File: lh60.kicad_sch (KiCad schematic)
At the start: 0 parts

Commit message: feat(sch): add production keyboard matrix
Co-authored-by: TRAE CLI <noreply@bytedance.com>
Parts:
- added D1, D10, D11, D12, D13, D14, D15, D16, D17, D18, D19, D2, D20, D21, D22, D23, D24, D25, D26, D27, D28, D29, D3, D30, D31, D32, D33, D34, D35, D36, D37, D38, D39, D4, D40, D41, D42, D43, D44, D45, D46, D47, D48, D49, D5, D50, D51, D52, D53, D54, D55, D56, D57, D58, D59, D6, D60, D61, D62, D63, D64, D65, D66, D67, D68, D69, D7, D70, D8, D9: 1N4148WS, lh60-core:D_SOD-323_Bottom, symbol lh60-core:MatrixDiode
- added SW1: r0_esc_1u, lh60-sockets:Gateron-LP-or-ChocV1-Hotswap-Socket-1U, symbol lh60-core:KeySwitch
- added SW10: r0_9_1u, lh60-sockets:Gateron-LP-or-ChocV1-Hotswap-Socket-1U, symbol lh60-core:KeySwitch
- added SW11: r0_0_1u, lh60-sockets:Gateron-LP-or-ChocV1-Hotswap-Socket-1U, symbol lh60-core:KeySwitch
- added SW12: r0_minus_1u, lh60-sockets:Gateron-LP-or-ChocV1-Hotswap-Socket-1U, symbol lh60-core:KeySwitch
- added SW13: r0_equal_1u, lh60-sockets:Gateron-LP-or-ChocV1-Hotswap-Socket-1U, symbol lh60-core:KeySwitch
- added SW14: r0_top_2u, lh60-sockets:Gateron-LP-Hotswap-Socket-2U, symbol lh60-core:KeySwitch
- added SW15: r0_top_split_left_fn_1u, lh60-sockets:Gateron-LP-Hotswap-Socket-1U, symbol lh60-core:KeySwitch
- added SW16: r0_top_split_right_1u, lh60-sockets:Gateron-LP-Hotswap-Socket-1U, symbol lh60-core:KeySwitch
- added SW17: r1_tab_1.5u, lh60-sockets:Gateron-LP-or-ChocV1-Hotswap-Socket-1.5U, symbol lh60-core:KeySwitch
- added SW18: r1_q_1u, lh60-sockets:Gateron-LP-or-ChocV1-Hotswap-Socket-1U, symbol lh60-core:KeySwitch
- added SW19: r1_w_1u, lh60-sockets:Gateron-LP-or-ChocV1-Hotswap-Socket-1U, symbol lh60-core:KeySwitch
- added SW2: r0_1_1u, lh60-sockets:Gateron-LP-or-ChocV1-Hotswap-Socket-1U, symbol lh60-core:KeySwitch
- added SW20: r1_e_1u, lh60-sockets:Gateron-LP-or-ChocV1-Hotswap-Socket-1U, symbol lh60-core:KeySwitch
- added SW21: r1_r_1u, lh60-sockets:Gateron-LP-or-ChocV1-Hotswap-Socket-1U, symbol lh60-core:KeySwitch
- added SW22: r1_t_1u, lh60-sockets:Gateron-LP-or-ChocV1-Hotswap-Socket-1U, symbol lh60-core:KeySwitch
- added SW23: r1_y_1u, lh60-sockets:Gateron-LP-or-ChocV1-Hotswap-Socket-1U, symbol lh60-core:KeySwitch
- added SW24: r1_u_1u, lh60-sockets:Gateron-LP-or-ChocV1-Hotswap-Socket-1U, symbol lh60-core:KeySwitch
- added SW25: r1_i_1u, lh60-sockets:Gateron-LP-or-ChocV1-Hotswap-Socket-1U, symbol lh60-core:KeySwitch
- added SW26: r1_o_1u, lh60-sockets:Gateron-LP-or-ChocV1-Hotswap-Socket-1U, symbol lh60-core:KeySwitch
- added SW27: r1_p_1u, lh60-sockets:Gateron-LP-or-ChocV1-Hotswap-Socket-1U, symbol lh60-core:KeySwitch
- added SW28: r1_left_bracket_1u, lh60-sockets:Gateron-LP-or-ChocV1-Hotswap-Socket-1U, symbol lh60-core:KeySwitch
- added SW29: r1_right_bracket_1u, lh60-sockets:Gateron-LP-or-ChocV1-Hotswap-Socket-1U, symbol lh60-core:KeySwitch
- added SW3: r0_2_1u, lh60-sockets:Gateron-LP-or-ChocV1-Hotswap-Socket-1U, symbol lh60-core:KeySwitch
- added SW30: r1_backslash_1.5u, lh60-sockets:Gateron-LP-or-ChocV1-Hotswap-Socket-1.5U, symbol lh60-core:KeySwitch
- added SW31: r2_caps_1.75u, lh60-sockets:Gateron-LP-or-ChocV1-Hotswap-Socket-1.75U, symbol lh60-core:KeySwitch
- added SW32: r2_a_1u, lh60-sockets:Gateron-LP-or-ChocV1-Hotswap-Socket-1U, symbol lh60-core:KeySwitch
- added SW33: r2_s_1u, lh60-sockets:Gateron-LP-or-ChocV1-Hotswap-Socket-1U, symbol lh60-core:KeySwitch
- added SW34: r2_d_1u, lh60-sockets:Gateron-LP-or-ChocV1-Hotswap-Socket-1U, symbol lh60-core:KeySwitch
- added SW35: r2_f_1u, lh60-sockets:Gateron-LP-or-ChocV1-Hotswap-Socket-1U, symbol lh60-core:KeySwitch
- added SW36: r2_g_1u, lh60-sockets:Gateron-LP-or-ChocV1-Hotswap-Socket-1U, symbol lh60-core:KeySwitch
- added SW37: r2_h_1u, lh60-sockets:Gateron-LP-or-ChocV1-Hotswap-Socket-1U, symbol lh60-core:KeySwitch
- added SW38: r2_j_1u, lh60-sockets:Gateron-LP-or-ChocV1-Hotswap-Socket-1U, symbol lh60-core:KeySwitch
- added SW39: r2_k_1u, lh60-sockets:Gateron-LP-or-ChocV1-Hotswap-Socket-1U, symbol lh60-core:KeySwitch
- added SW4: r0_3_1u, lh60-sockets:Gateron-LP-or-ChocV1-Hotswap-Socket-1U, symbol lh60-core:KeySwitch
- added SW40: r2_l_1u, lh60-sockets:Gateron-LP-or-ChocV1-Hotswap-Socket-1U, symbol lh60-core:KeySwitch
- added SW41: r2_semicolon_1u, lh60-sockets:Gateron-LP-or-ChocV1-Hotswap-Socket-1U, symbol lh60-core:KeySwitch
- added SW42: r2_quote_1u, lh60-sockets:Gateron-LP-or-ChocV1-Hotswap-Socket-1U, symbol lh60-core:KeySwitch
- added SW43: r2_enter_ansi_2.25u, lh60-sockets:Gateron-LP-Hotswap-Socket-2.25U, symbol lh60-core:KeySwitch
- added SW44: r2_enter_split_left_fn_1u, lh60-sockets:Gateron-LP-Hotswap-Socket-1U, symbol lh60-core:KeySwitch
- added SW45: r2_enter_split_right_1.25u, lh60-sockets:Gateron-LP-Hotswap-Socket-1.25U, symbol lh60-core:KeySwitch
- added SW46: r3_lshift_split_left_fn_1u, lh60-sockets:Gateron-LP-Hotswap-Socket-1U, symbol lh60-core:KeySwitch
- added SW47: r3_lshift_2.25u, lh60-sockets:Gateron-LP-Hotswap-Socket-2.25U, symbol lh60-core:KeySwitch
- added SW48: r3_lshift_split_1.25u, lh60-sockets:Gateron-LP-Hotswap-Socket-1.25U, symbol lh60-core:KeySwitch
- added SW49: r3_z_1u, lh60-sockets:Gateron-LP-or-ChocV1-Hotswap-Socket-1U, symbol lh60-core:KeySwitch
- added SW5: r0_4_1u, lh60-sockets:Gateron-LP-or-ChocV1-Hotswap-Socket-1U, symbol lh60-core:KeySwitch
- added SW50: r3_x_1u, lh60-sockets:Gateron-LP-or-ChocV1-Hotswap-Socket-1U, symbol lh60-core:KeySwitch
- added SW51: r3_c_1u, lh60-sockets:Gateron-LP-or-ChocV1-Hotswap-Socket-1U, symbol lh60-core:KeySwitch
- added SW52: r3_v_1u, lh60-sockets:Gateron-LP-or-ChocV1-Hotswap-Socket-1U, symbol lh60-core:KeySwitch
- added SW53: r3_b_1u, lh60-sockets:Gateron-LP-or-ChocV1-Hotswap-Socket-1U, symbol lh60-core:KeySwitch
- added SW54: r3_n_1u, lh60-sockets:Gateron-LP-or-ChocV1-Hotswap-Socket-1U, symbol lh60-core:KeySwitch
- added SW55: r3_m_1u, lh60-sockets:Gateron-LP-or-ChocV1-Hotswap-Socket-1U, symbol lh60-core:KeySwitch
- added SW56: r3_comma_1u, lh60-sockets:Gateron-LP-or-ChocV1-Hotswap-Socket-1U, symbol lh60-core:KeySwitch
- added SW57: r3_period_1u, lh60-sockets:Gateron-LP-or-ChocV1-Hotswap-Socket-1U, symbol lh60-core:KeySwitch
- added SW58: r3_slash_1u, lh60-sockets:Gateron-LP-or-ChocV1-Hotswap-Socket-1U, symbol lh60-core:KeySwitch
- added SW59: r3_rshift_2.75u, lh60-sockets:Gateron-LP-Hotswap-Socket-2.75U, symbol lh60-core:KeySwitch
- added SW6: r0_5_1u, lh60-sockets:Gateron-LP-or-ChocV1-Hotswap-Socket-1U, symbol lh60-core:KeySwitch
- added SW60: r3_rshift_left_1.75u, lh60-sockets:Gateron-LP-Hotswap-Socket-1.75U, symbol lh60-core:KeySwitch
- added SW61: r3_rshift_right_fn_1u, lh60-sockets:Gateron-LP-Hotswap-Socket-1U, symbol lh60-core:KeySwitch
- added SW62: r3_rshift_left_fn_1u, lh60-sockets:Gateron-LP-Hotswap-Socket-1U, symbol lh60-core:KeySwitch
- added SW63: r3_rshift_right_1.75u, lh60-sockets:Gateron-LP-Hotswap-Socket-1.75U, symbol lh60-core:KeySwitch
- added SW64: r4_left_ctrl_1.25u, lh60-sockets:Gateron-LP-or-ChocV1-Hotswap-Socket-1.25U, symbol lh60-core:KeySwitch
- added SW65: r4_left_win_1.25u, lh60-sockets:Gateron-LP-or-ChocV1-Hotswap-Socket-1.25U, symbol lh60-core:KeySwitch
- added SW66: r4_left_alt_1.25u, lh60-sockets:Gateron-LP-or-ChocV1-Hotswap-Socket-1.25U, symbol lh60-core:KeySwitch
- added SW67: r4_space_2.25u, lh60-sockets:Gateron-LP-or-ChocV1-Hotswap-Socket-2.25U, symbol lh60-core:KeySwitch
- added SW68: r4_fn_1u, lh60-sockets:Gateron-LP-or-ChocV1-Hotswap-Socket-1U, symbol lh60-core:KeySwitch
- added SW69: r4_left_1u, lh60-sockets:Gateron-LP-or-ChocV1-Hotswap-Socket-1U, symbol lh60-core:KeySwitch
- added SW7: r0_6_1u, lh60-sockets:Gateron-LP-or-ChocV1-Hotswap-Socket-1U, symbol lh60-core:KeySwitch
- added SW70: r4_down_1u, lh60-sockets:Gateron-LP-or-ChocV1-Hotswap-Socket-1U, symbol lh60-core:KeySwitch
- added SW71: r4_up_1u, lh60-sockets:Gateron-LP-or-ChocV1-Hotswap-Socket-1U, symbol lh60-core:KeySwitch
- added SW72: r4_right_1u, lh60-sockets:Gateron-LP-or-ChocV1-Hotswap-Socket-1U, symbol lh60-core:KeySwitch
- added SW73: r4_right_fn_1u, lh60-sockets:Gateron-LP-or-ChocV1-Hotswap-Socket-1U, symbol lh60-core:KeySwitch
- added SW74: r4_right_alt_1u, lh60-sockets:Gateron-LP-or-ChocV1-Hotswap-Socket-1U, symbol lh60-core:KeySwitch
- added SW75: r4_right_win_1u, lh60-sockets:Gateron-LP-or-ChocV1-Hotswap-Socket-1U, symbol lh60-core:KeySwitch
- added SW76: r4_right_ctrl_1u, lh60-sockets:Gateron-LP-or-ChocV1-Hotswap-Socket-1U, symbol lh60-core:KeySwitch
- added SW8: r0_7_1u, lh60-sockets:Gateron-LP-or-ChocV1-Hotswap-Socket-1U, symbol lh60-core:KeySwitch
- added SW9: r0_8_1u, lh60-sockets:Gateron-LP-or-ChocV1-Hotswap-Socket-1U, symbol lh60-core:KeySwitch
- added TP1: VSYS, lh60-core:TestPoint_Pad_D1.5mm_Bottom, symbol lh60-core:TestPoint
- added TP10: COL6, lh60-core:TestPoint_Pad_D1.5mm_Bottom, symbol lh60-core:TestPoint
- added TP11: COL7, lh60-core:TestPoint_Pad_D1.5mm_Bottom, symbol lh60-core:TestPoint
- added TP12: COL8, lh60-core:TestPoint_Pad_D1.5mm_Bottom, symbol lh60-core:TestPoint
- added TP13: COL9, lh60-core:TestPoint_Pad_D1.5mm_Bottom, symbol lh60-core:TestPoint
- added TP14: ROW0, lh60-core:TestPoint_Pad_D1.5mm_Bottom, symbol lh60-core:TestPoint
- added TP15: ROW1, lh60-core:TestPoint_Pad_D1.5mm_Bottom, symbol lh60-core:TestPoint
- added TP16: ROW2, lh60-core:TestPoint_Pad_D1.5mm_Bottom, symbol lh60-core:TestPoint
- added TP17: ROW3, lh60-core:TestPoint_Pad_D1.5mm_Bottom, symbol lh60-core:TestPoint
- added TP18: ROW4, lh60-core:TestPoint_Pad_D1.5mm_Bottom, symbol lh60-core:TestPoint
- added TP19: ROW5, lh60-core:TestPoint_Pad_D1.5mm_Bottom, symbol lh60-core:TestPoint
- added TP2: 3V3, lh60-core:TestPoint_Pad_D1.5mm_Bottom, symbol lh60-core:TestPoint
- added TP20: ROW6, lh60-core:TestPoint_Pad_D1.5mm_Bottom, symbol lh60-core:TestPoint
- added TP21: GP27, lh60-core:TestPoint_Pad_D1.5mm_Bottom, symbol lh60-core:TestPoint
- added TP22: GP28, lh60-core:TestPoint_Pad_D1.5mm_Bottom, symbol lh60-core:TestPoint
- added TP23: GP29, lh60-core:TestPoint_Pad_D1.5mm_Bottom, symbol lh60-core:TestPoint
- added TP3: GND, lh60-core:TestPoint_Pad_D1.5mm_Bottom, symbol lh60-core:TestPoint
- added TP4: COL0, lh60-core:TestPoint_Pad_D1.5mm_Bottom, symbol lh60-core:TestPoint
- added TP5: COL1, lh60-core:TestPoint_Pad_D1.5mm_Bottom, symbol lh60-core:TestPoint
- added TP6: COL2, lh60-core:TestPoint_Pad_D1.5mm_Bottom, symbol lh60-core:TestPoint
- added TP7: COL3, lh60-core:TestPoint_Pad_D1.5mm_Bottom, symbol lh60-core:TestPoint
- added TP8: COL4, lh60-core:TestPoint_Pad_D1.5mm_Bottom, symbol lh60-core:TestPoint
- added TP9: COL5, lh60-core:TestPoint_Pad_D1.5mm_Bottom, symbol lh60-core:TestPoint
- added U1: RP2040-Tiny, lh60-mcu:MCU_RP2040-Tiny_SMD, symbol lh60-mcu:RP2040-Tiny
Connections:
- new net 3V3: TP2.1 (TP), U1.21 (3V3)
- new net COL0: D1.2 (A), D11.2 (A), D21.2 (A), D31.2 (A), D41.2 (A), D51.2 (A), D61.2 (A), TP4.1 (TP), U1.1 (GP0)
- new net COL1: D12.2 (A), D2.2 (A), D22.2 (A), D32.2 (A), D42.2 (A), D52.2 (A), D62.2 (A), TP5.1 (TP), U1.2 (GP1)
- new net COL2: D13.2 (A), D23.2 (A), D3.2 (A), D33.2 (A), D43.2 (A), D53.2 (A), D63.2 (A), TP6.1 (TP), U1.3 (GP2)
- new net COL3: D14.2 (A), D24.2 (A), D34.2 (A), D4.2 (A), D44.2 (A), D54.2 (A), D64.2 (A), TP7.1 (TP), U1.4 (GP3)
- new net COL4: D15.2 (A), D25.2 (A), D35.2 (A), D45.2 (A), D5.2 (A), D55.2 (A), D65.2 (A), TP8.1 (TP), U1.5 (GP4)
- new net COL5: D16.2 (A), D26.2 (A), D36.2 (A), D46.2 (A), D56.2 (A), D6.2 (A), D66.2 (A), TP9.1 (TP), U1.6 (GP5)
- new net COL6: D17.2 (A), D27.2 (A), D37.2 (A), D47.2 (A), D57.2 (A), D67.2 (A), D7.2 (A), TP10.1 (TP), U1.7 (GP6)
- new net COL7: D18.2 (A), D28.2 (A), D38.2 (A), D48.2 (A), D58.2 (A), D68.2 (A), D8.2 (A), TP11.1 (TP), U1.8 (GP7)
- new net COL8: D19.2 (A), D29.2 (A), D39.2 (A), D49.2 (A), D59.2 (A), D69.2 (A), D9.2 (A), TP12.1 (TP), U1.9 (GP8)
- new net COL9: D10.2 (A), D20.2 (A), D30.2 (A), D40.2 (A), D50.2 (A), D60.2 (A), D70.2 (A), TP13.1 (TP), U1.10 (GP9)
- new net GND: TP3.1 (TP), U1.22 (GND)
- new net GP27: TP21.1 (TP), U1.18 (GP27)
- new net GP28: TP22.1 (TP), U1.19 (GP28)
- new net GP29: TP23.1 (TP), U1.20 (GP29)
- new net KEY_00: D1.1 (K), SW1.1
- new net KEY_01: D2.1 (K), SW2.1
- new net KEY_02: D3.1 (K), SW3.1
- new net KEY_03: D4.1 (K), SW4.1
- new net KEY_04: D5.1 (K), SW5.1
- new net KEY_05: D6.1 (K), SW6.1
- new net KEY_06: D7.1 (K), SW7.1
- new net KEY_07: D8.1 (K), SW8.1
- new net KEY_08: D9.1 (K), SW9.1
- new net KEY_09: D10.1 (K), SW10.1
- new net KEY_10: D11.1 (K), SW11.1
- new net KEY_11: D12.1 (K), SW12.1
- new net KEY_12: D13.1 (K), SW13.1
- new net KEY_13: D14.1 (K), SW14.1, SW16.1
- new net KEY_14: D15.1 (K), SW15.1
- new net KEY_15: D16.1 (K), SW17.1
- new net KEY_16: D17.1 (K), SW18.1
- new net KEY_17: D18.1 (K), SW19.1
- new net KEY_18: D19.1 (K), SW20.1
- new net KEY_19: D20.1 (K), SW21.1
- new net KEY_20: D21.1 (K), SW22.1
- new net KEY_21: D22.1 (K), SW23.1
- new net KEY_22: D23.1 (K), SW24.1
- new net KEY_23: D24.1 (K), SW25.1
- new net KEY_24: D25.1 (K), SW26.1
- new net KEY_25: D26.1 (K), SW27.1
- new net KEY_26: D27.1 (K), SW28.1
- new net KEY_27: D28.1 (K), SW29.1
- new net KEY_28: D29.1 (K), SW30.1
- new net KEY_29: D30.1 (K), SW31.1
- new net KEY_30: D31.1 (K), SW32.1
- new net KEY_31: D32.1 (K), SW33.1
- new net KEY_32: D33.1 (K), SW34.1
- new net KEY_33: D34.1 (K), SW35.1
- new net KEY_34: D35.1 (K), SW36.1
- new net KEY_35: D36.1 (K), SW37.1
- new net KEY_36: D37.1 (K), SW38.1
- new net KEY_37: D38.1 (K), SW39.1
- new net KEY_38: D39.1 (K), SW40.1
- new net KEY_39: D40.1 (K), SW41.1
- new net KEY_40: D41.1 (K), SW42.1
- new net KEY_41: D42.1 (K), SW43.1, SW45.1
- new net KEY_42: D43.1 (K), SW44.1
- new net KEY_43: D44.1 (K), SW46.1
- new net KEY_44: D45.1 (K), SW47.1, SW48.1
- new net KEY_45: D46.1 (K), SW49.1
- new net KEY_46: D47.1 (K), SW50.1
- new net KEY_47: D48.1 (K), SW51.1
- new net KEY_48: D49.1 (K), SW52.1
- new net KEY_49: D50.1 (K), SW53.1
- new net KEY_50: D51.1 (K), SW54.1
- new net KEY_51: D52.1 (K), SW55.1
- new net KEY_52: D53.1 (K), SW56.1
- new net KEY_53: D54.1 (K), SW57.1
- new net KEY_54: D55.1 (K), SW58.1
- new net KEY_55: D56.1 (K), SW59.1, SW60.1, SW63.1
- new net KEY_56: D57.1 (K), SW61.1, SW62.1
- new net KEY_57: D58.1 (K), SW64.1
- new net KEY_58: D59.1 (K), SW65.1
- new net KEY_59: D60.1 (K), SW66.1
- new net KEY_60: D61.1 (K), SW67.1
- new net KEY_61: D62.1 (K), SW68.1
- new net KEY_62: D63.1 (K), SW69.1
- new net KEY_63: D64.1 (K), SW70.1
- new net KEY_64: D65.1 (K), SW71.1
- new net KEY_65: D66.1 (K), SW72.1
- new net KEY_66: D67.1 (K), SW73.1
- new net KEY_67: D68.1 (K), SW74.1
- new net KEY_68: D69.1 (K), SW75.1
- new net KEY_69: D70.1 (K), SW76.1
- new net ROW0: SW1.2, SW10.2, SW2.2, SW3.2, SW4.2, SW5.2, SW6.2, SW7.2, SW8.2, SW9.2, TP14.1 (TP), U1.11 (GP10)
- new net ROW1: SW11.2, SW12.2, SW13.2, SW14.2, SW15.2, SW16.2, SW17.2, SW18.2, SW19.2, SW20.2, SW21.2, TP15.1 (TP), U1.12 (GP11)
- new net ROW2: SW22.2, SW23.2, SW24.2, SW25.2, SW26.2, SW27.2, SW28.2, SW29.2, SW30.2, SW31.2, TP16.1 (TP), U1.13 (GP12)
- new net ROW3: SW32.2, SW33.2, SW34.2, SW35.2, SW36.2, SW37.2, SW38.2, SW39.2, SW40.2, SW41.2, TP17.1 (TP), U1.14 (GP13)
- new net ROW4: SW42.2, SW43.2, SW44.2, SW45.2, SW46.2, SW47.2, SW48.2, SW49.2, SW50.2, SW51.2, SW52.2, SW53.2, TP18.1 (TP), U1.15 (GP14)
- new net ROW5: SW54.2, SW55.2, SW56.2, SW57.2, SW58.2, SW59.2, SW60.2, SW61.2, SW62.2, SW63.2, SW64.2, SW65.2, SW66.2, TP19.1 (TP), U1.16 (GP15)
- new net ROW6: SW67.2, SW68.2, SW69.2, SW70.2, SW71.2, SW72.2, SW73.2, SW74.2, SW75.2, SW76.2, TP20.1 (TP), U1.17 (GP26)
- new net VSYS: TP1.1 (TP), U1.23 (VSYS)

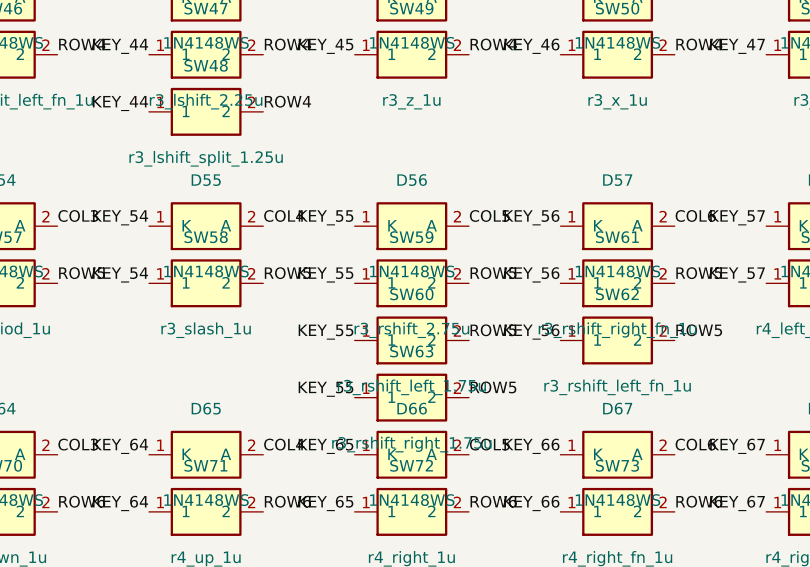
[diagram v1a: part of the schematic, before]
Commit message: refactor(layout): retire RShift 2.75u option
Remove the retired SW59 schematic path while preserving later switch references, refresh production region reports, and update layout documentation and verification gates for the 75-socket contract.

Co-authored-by: TRAE CLI <noreply@bytedance.com>
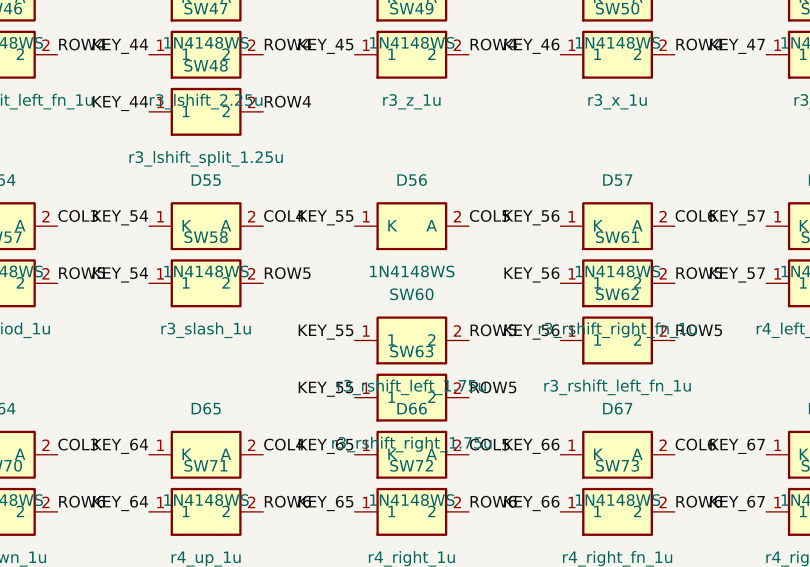
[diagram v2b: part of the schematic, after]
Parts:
- removed SW59: r3_rshift_2.75u, lh60-sockets:Gateron-LP-Hotswap-Socket-2.75U, symbol lh60-core:KeySwitch
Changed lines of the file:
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@@
 )
   (label "ROW5"
-    (at 135.89 148.59 0)
-    (effects
-      (font
-        (size 1.27 1.27))
-      (justify left bottom))
-)
-  (label "ROW5"
     (at 135.89 154.94 0)
     (effects
@@
 )
   (label "KEY_55"
-    (at 123.19 148.59 180)
-    (effects
-      (font
-        (size 1.27 1.27))
-      (justify right bottom))
-)
-  (label "KEY_55"
     (at 123.19 154.94 180)
     (effects
@@
           (unit 1)))))
   (symbol
-    (lib_id "lh60-core:KeySwitch")
-    (at 129.54 148.59 0)
-    (unit 1)
-    (in_bom yes)
-    (on_board yes)
-    (dnp no)
-    (property "Reference" "SW59"
-      (at 129.54 143.51 0)
-      (effects
-        (font
-          (size 1.27 1.27))))
-    (property "Value" "r3_rshift_2.75u"
-      (at 129.54 153.67 0)
-      (effects
-        (font
-          (size 1.27 1.27))))
-    (property "Footprint" "lh60-sockets:Gateron-LP-Hotswap-Socket-2.75U"
-      (at 129.54 148.59 0)
-      (hide yes)
-      (effects
-        (font
-          (size 1.27 1.27))))
-    (property "Datasheet" ""
-      (at 129.54 148.59 0)
-      (hide yes)
-      (effects
-        (font
-          (size 1.27 1.27))))
-    (instances
-      (project "lh60"
-        (path "/1ff94ced-4ad0-4573-85e6-3ea048ef8c2d"
-          (reference "SW59")
-          (unit 1)))))
-  (symbol

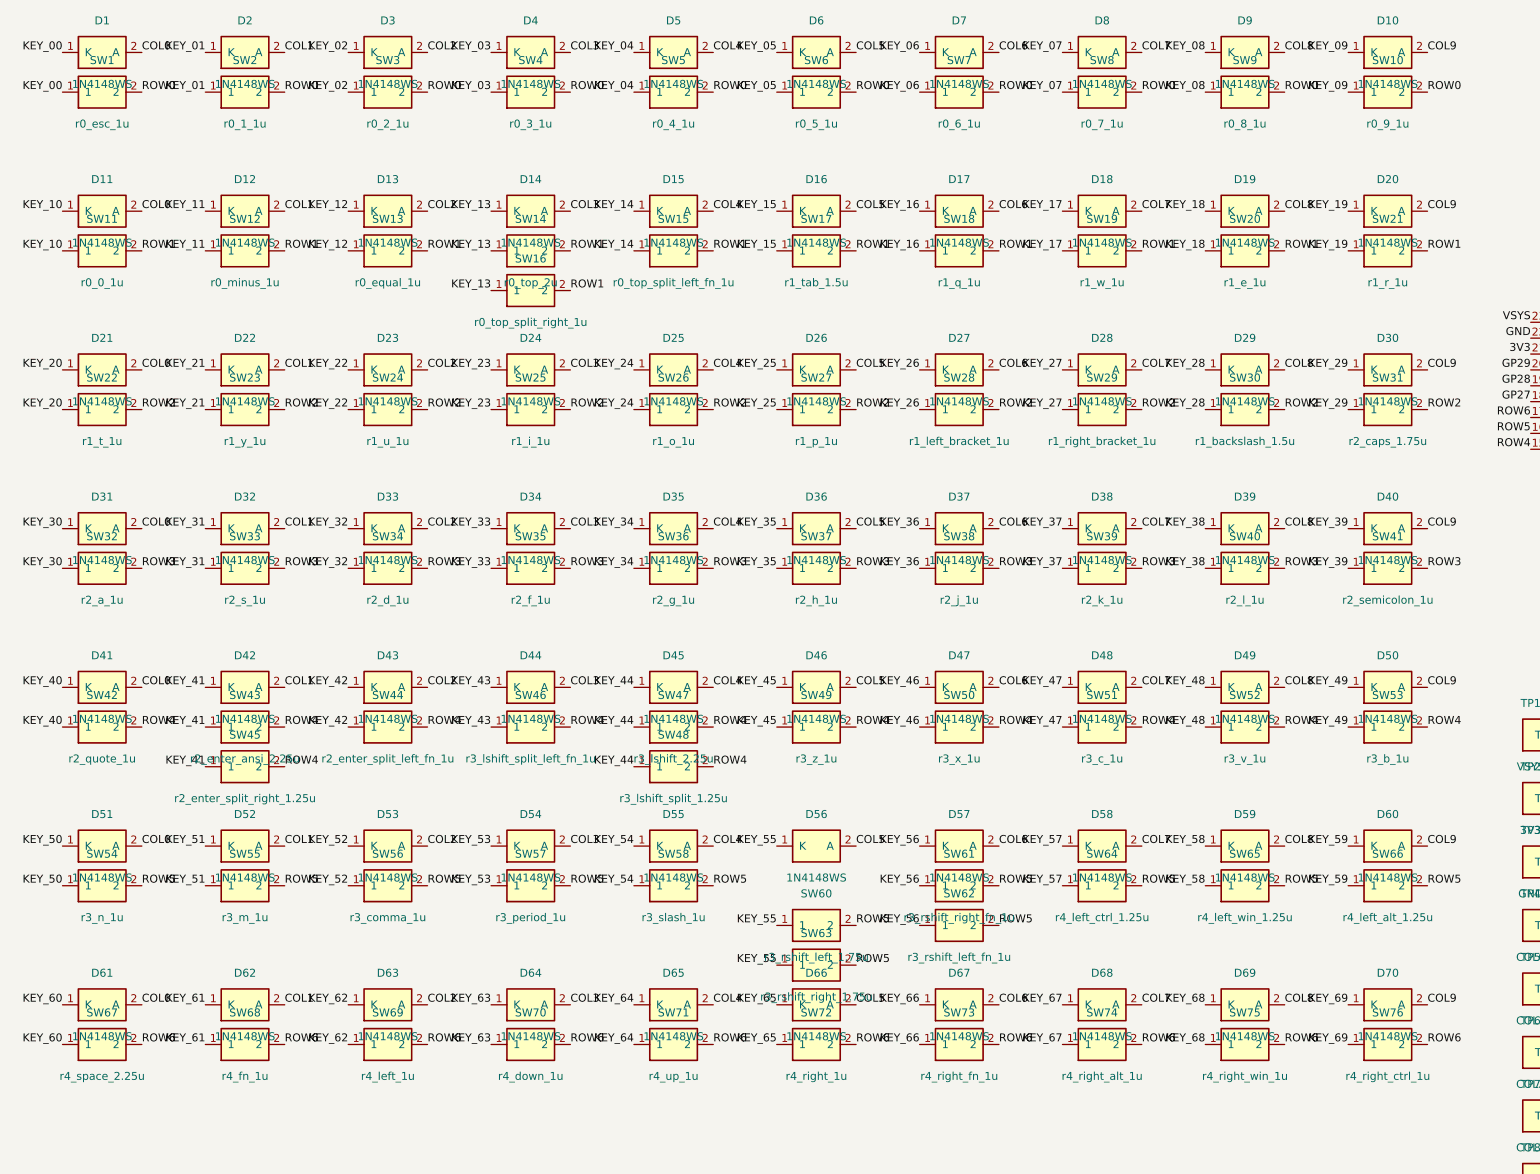
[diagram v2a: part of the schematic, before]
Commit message: refactor(schematic): use default switch and diode symbols
Replace all placed switches with Switch:SW_Push and all matrix diodes with Device:D while preserving references, values, footprints, placement, and connectivity. Remove the retired project-local symbol definitions and keep support symbols and custom footprints in lh60-core.

Co-authored-by: TRAE CLI <noreply@bytedance.com>
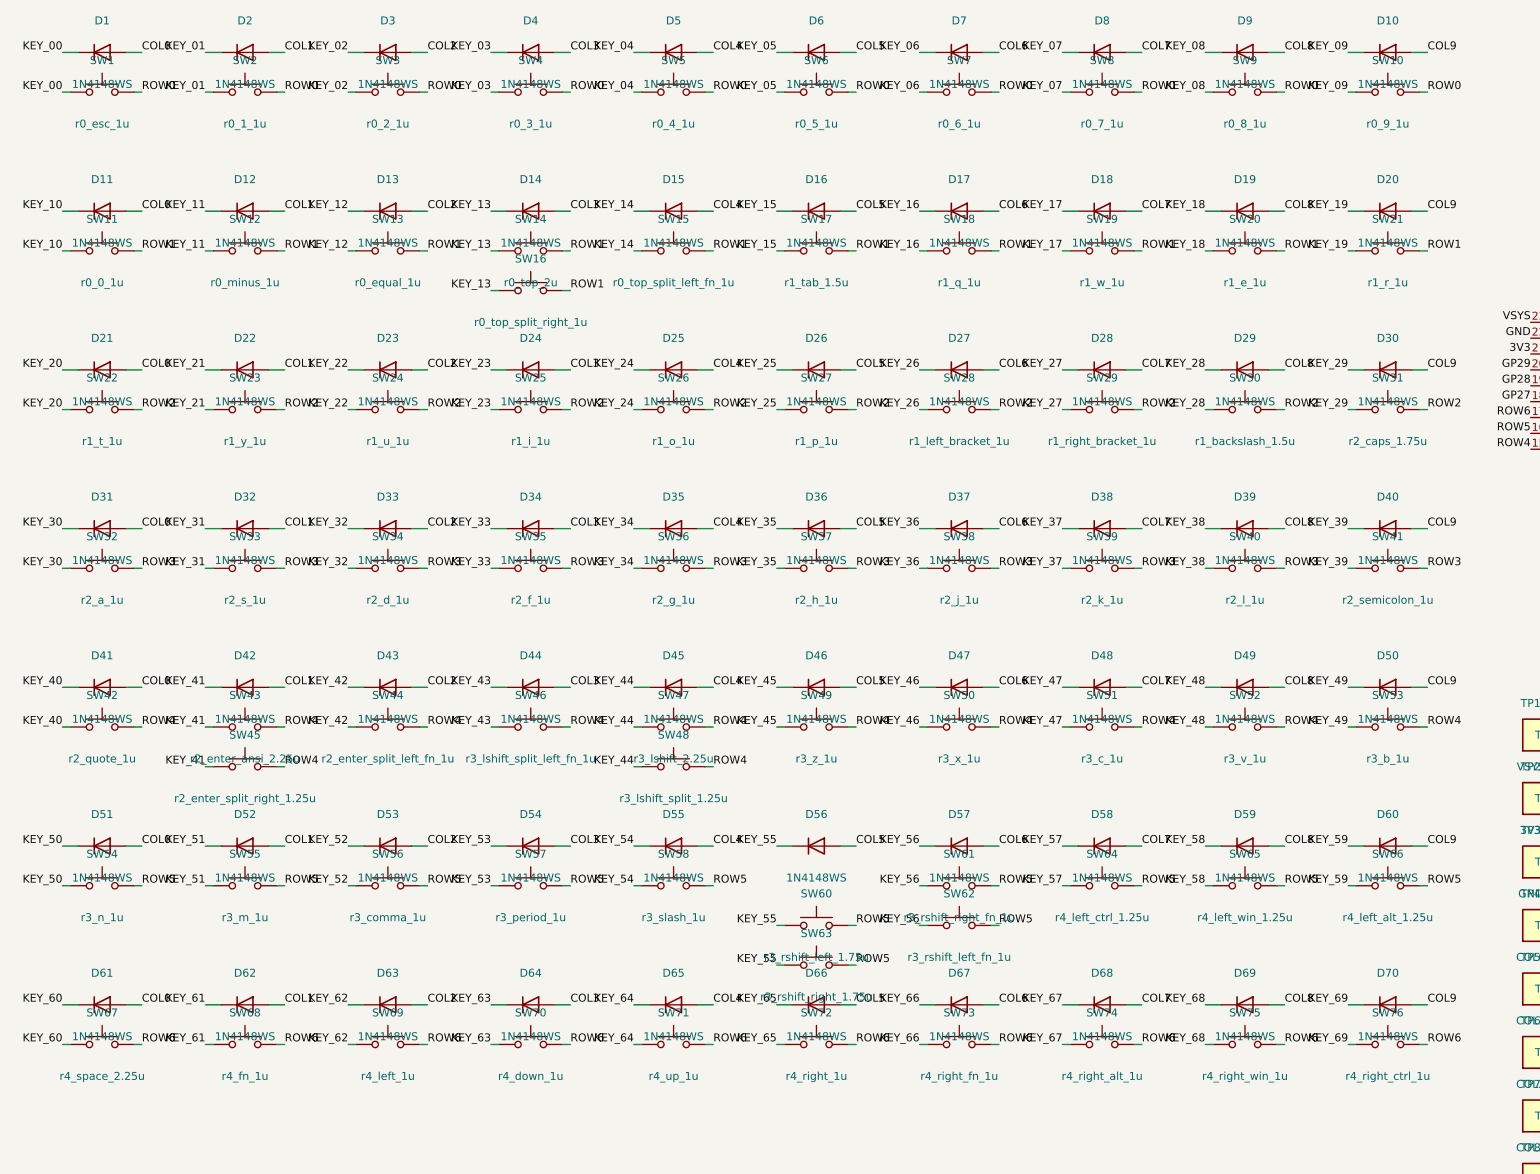
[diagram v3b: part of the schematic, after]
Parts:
- D1, D10, D11, D12, D13, D14, D15, D16, D17, D18, D19, D2, D20, D21, D22, D23, D24, D25, D26, D27, D28, D29, D3, D30, D31, D32, D33, D34, D35, D36, D37, D38, D39, D4, D40, D41, D42, D43, D44, D45, D46, D47, D48, D49, D5, D50, D51, D52, D53, D54, D55, D56, D57, D58, D59, D6, D60, D61, D62, D63, D64, D65, D66, D67, D68, D69, D7, D70, D8, D9: symbol lh60-core:MatrixDiode -> Device:D
- SW1, SW10, SW11, SW12, SW13, SW14, SW15, SW16, SW17, SW18, SW19, SW2, SW20, SW21, SW22, SW23, SW24, SW25, SW26, SW27, SW28, SW29, SW3, SW30, SW31, SW32, SW33, SW34, SW35, SW36, SW37, SW38, SW39, SW4, SW40, SW41, SW42, SW43, SW44, SW45, SW46, SW47, SW48, SW49, SW5, SW50, SW51, SW52, SW53, SW54, SW55, SW56, SW57, SW58, SW6, SW60, SW61, SW62, SW63, SW64, SW65, SW66, SW67, SW68, SW69, SW7, SW70, SW71, SW72, SW73, SW74, SW75, SW76, SW8, SW9: symbol lh60-core:KeySwitch -> Switch:SW_Push

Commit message: refactor(schematic): group debug headers on A3
Co-authored-by: TRAE CLI <noreply@bytedance.com>
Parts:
- removed TP1: VSYS, lh60-core:TestPoint_Pad_D1.5mm_Bottom, symbol lh60-core:TestPoint
- removed TP10: COL6, lh60-core:TestPoint_Pad_D1.5mm_Bottom, symbol lh60-core:TestPoint
- removed TP11: COL7, lh60-core:TestPoint_Pad_D1.5mm_Bottom, symbol lh60-core:TestPoint
- removed TP12: COL8, lh60-core:TestPoint_Pad_D1.5mm_Bottom, symbol lh60-core:TestPoint
- removed TP13: COL9, lh60-core:TestPoint_Pad_D1.5mm_Bottom, symbol lh60-core:TestPoint
- removed TP14: ROW0, lh60-core:TestPoint_Pad_D1.5mm_Bottom, symbol lh60-core:TestPoint
- removed TP15: ROW1, lh60-core:TestPoint_Pad_D1.5mm_Bottom, symbol lh60-core:TestPoint
- removed TP16: ROW2, lh60-core:TestPoint_Pad_D1.5mm_Bottom, symbol lh60-core:TestPoint
- removed TP17: ROW3, lh60-core:TestPoint_Pad_D1.5mm_Bottom, symbol lh60-core:TestPoint
- removed TP18: ROW4, lh60-core:TestPoint_Pad_D1.5mm_Bottom, symbol lh60-core:TestPoint
- removed TP19: ROW5, lh60-core:TestPoint_Pad_D1.5mm_Bottom, symbol lh60-core:TestPoint
- removed TP2: 3V3, lh60-core:TestPoint_Pad_D1.5mm_Bottom, symbol lh60-core:TestPoint
- removed TP20: ROW6, lh60-core:TestPoint_Pad_D1.5mm_Bottom, symbol lh60-core:TestPoint
- removed TP21: GP27, lh60-core:TestPoint_Pad_D1.5mm_Bottom, symbol lh60-core:TestPoint
- removed TP22: GP28, lh60-core:TestPoint_Pad_D1.5mm_Bottom, symbol lh60-core:TestPoint
- removed TP23: GP29, lh60-core:TestPoint_Pad_D1.5mm_Bottom, symbol lh60-core:TestPoint
- removed TP3: GND, lh60-core:TestPoint_Pad_D1.5mm_Bottom, symbol lh60-core:TestPoint
- removed TP4: COL0, lh60-core:TestPoint_Pad_D1.5mm_Bottom, symbol lh60-core:TestPoint
- removed TP5: COL1, lh60-core:TestPoint_Pad_D1.5mm_Bottom, symbol lh60-core:TestPoint
- removed TP6: COL2, lh60-core:TestPoint_Pad_D1.5mm_Bottom, symbol lh60-core:TestPoint
- removed TP7: COL3, lh60-core:TestPoint_Pad_D1.5mm_Bottom, symbol lh60-core:TestPoint
- removed TP8: COL4, lh60-core:TestPoint_Pad_D1.5mm_Bottom, symbol lh60-core:TestPoint
- removed TP9: COL5, lh60-core:TestPoint_Pad_D1.5mm_Bottom, symbol lh60-core:TestPoint
- added J1: PWR, lh60-core:PinHeader_1x03_P2.54mm_Vertical, symbol lh60-core:Conn_01x03
- added J2: COL_A, lh60-core:PinHeader_1x05_P2.54mm_Vertical, symbol lh60-core:Conn_01x05
- added J3: COL_B, lh60-core:PinHeader_1x05_P2.54mm_Vertical, symbol lh60-core:Conn_01x05
- added J4: ROW_A, lh60-core:PinHeader_1x04_P2.54mm_Vertical, symbol lh60-core:Conn_01x04
- added J5: ROW_B, lh60-core:PinHeader_1x03_P2.54mm_Vertical, symbol lh60-core:Conn_01x03
- added J6: AUX, lh60-core:PinHeader_1x03_P2.54mm_Vertical, symbol lh60-core:Conn_01x03
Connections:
- net 3V3: now also J1.2
- net COL0: now also J2.1
- net COL1: now also J2.2
- net COL2: now also J2.3
- net COL3: now also J2.4
- net COL4: now also J2.5
- net COL5: now also J3.1
- net COL6: now also J3.2
- net COL7: now also J3.3
- net COL8: now also J3.4
- net COL9: now also J3.5
- net GND: now also J1.3
- net GP27: now also J6.1
- net GP28: now also J6.2
- net GP29: now also J6.3
- net ROW0: now also J4.1
- net ROW1: now also J4.2
- net ROW2: now also J4.3
- net ROW3: now also J4.4
- net ROW4: now also J5.1
- net ROW5: now also J5.2
- net ROW6: now also J5.3
- net VSYS: now also J1.1
